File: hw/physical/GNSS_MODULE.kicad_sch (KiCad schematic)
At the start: 16 parts, among them J3 Conn_Coaxial, U3 MAX-M8C

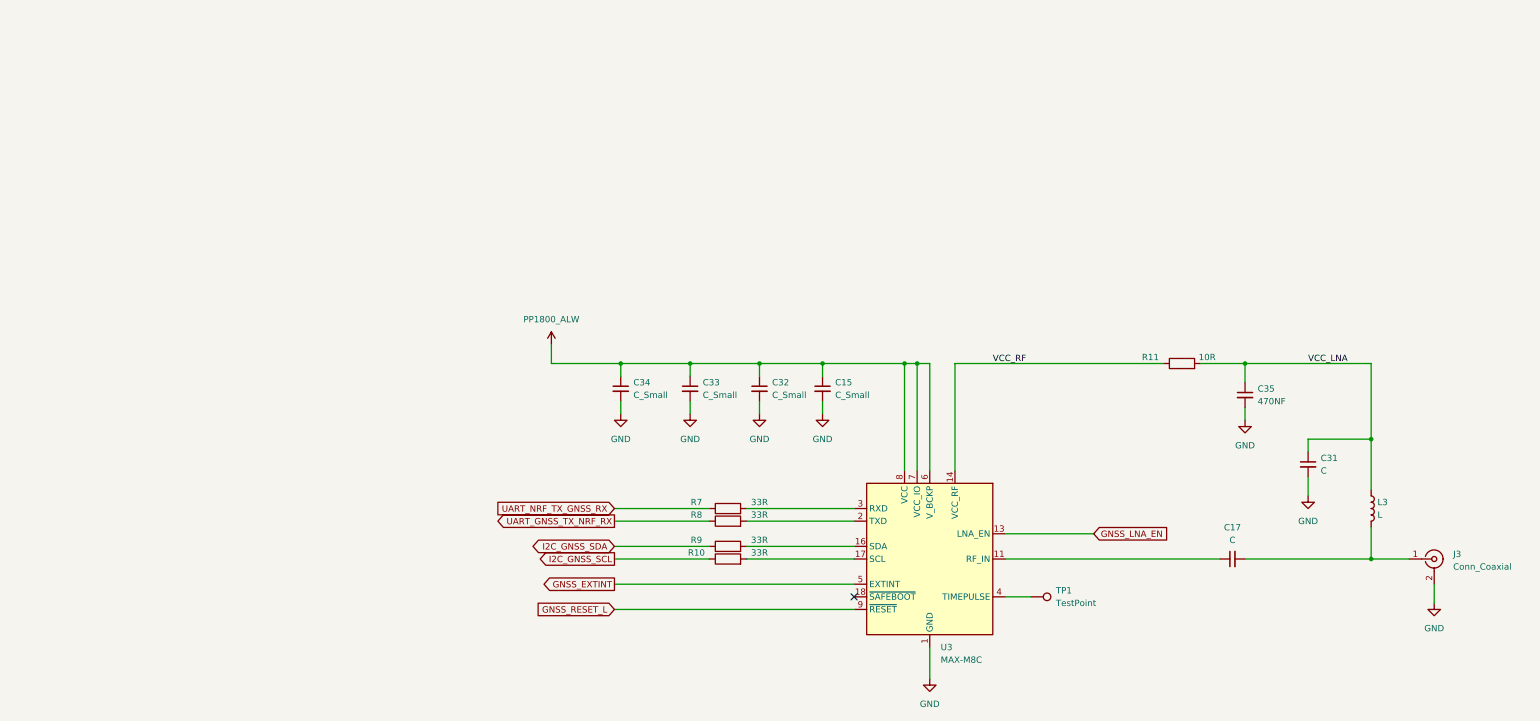
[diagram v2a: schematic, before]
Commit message: Various Schematic Modifications and Additions. * Removed Bypass page and moved bypass caps to MCU page. * Moved MCU VSS_PA pin to logical location as per Nordic guidelines. * Added Display Circuit, level shifters, charge pump, connector, etc. * Added 3.3V display VREG with Enable GPIO. * Added BLE RF components as per Nordic guidelines. * Added DCC circuit as per Nordic guidelines. * Rearranged GPIO's and interfaces. * Fixed various schematic errors.
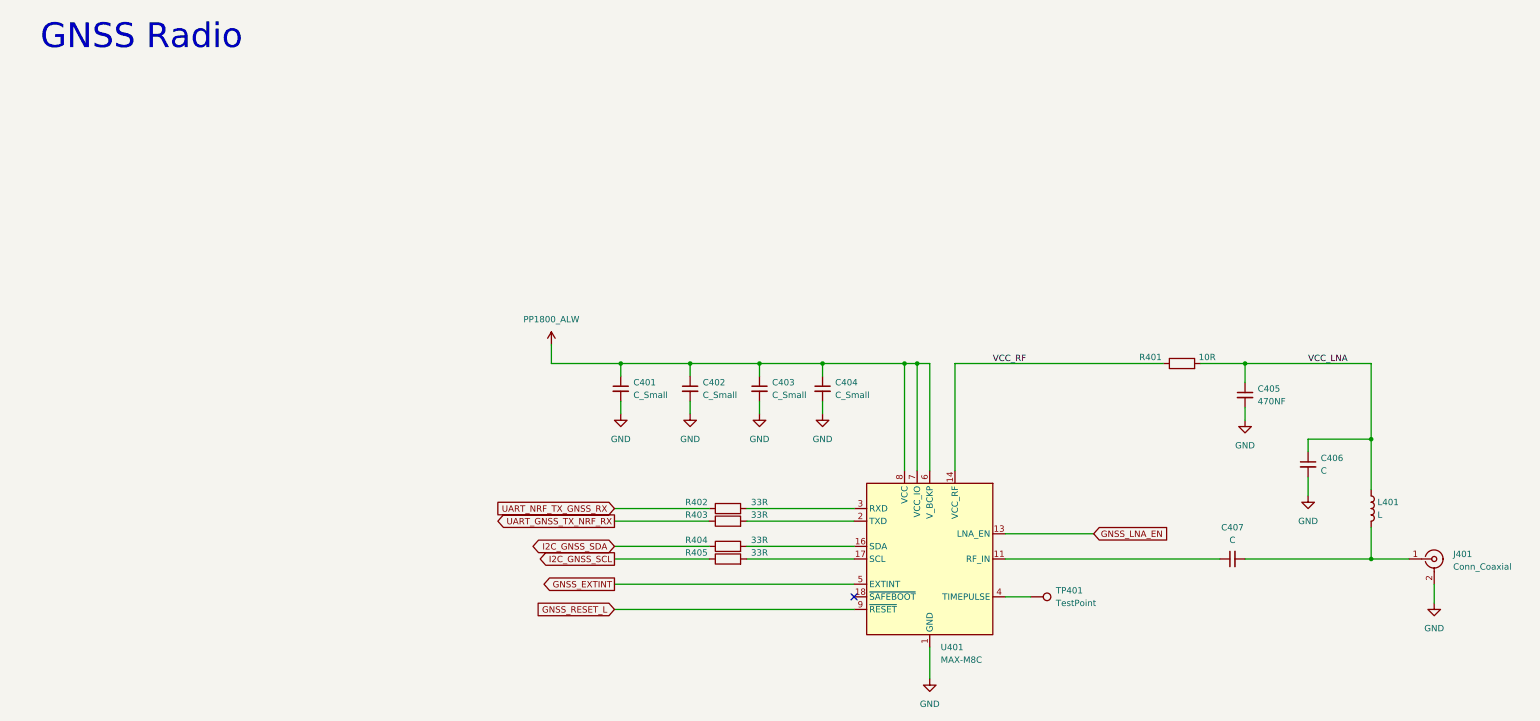
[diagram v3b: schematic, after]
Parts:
- renumbered C34 to C401, C33 to C402, C32 to C403, C15 to C404, C35 to C405, C31 to C406, C17 to C407, J3 to J401, L3 to L401, R11 to R401, R7 to R402, R8 to R403, R9 to R404, R10 to R405, TP1 to TP401, U3 to U401
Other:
- note added: "GNSS Radio"
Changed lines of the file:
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@@
+		)
+	)
+	(text "GNSS Radio"
+		(exclude_from_sim no)
+		(at 44.45 23.114 0)
+		(effects
+			(font
+				(size 5 5)
+			)
 		)
 	)
@@
 		(dnp no)
 		(fields_autoplaced yes)
-		(property "Reference" "#PWR038"
+		(property "Reference" "#PWR0408"
 			(at 304.8 143.51 0)
 			(effects
@@
 			(project "lora_radio_lp"
 				(path "/fff85bc4-e8ec-4b5d-b2e2-83ecb397a864/43b1fc22-b706-4706-a6f5-d4b7f0f9014a"
-					(reference "#PWR038")
+					(reference "#PWR0408")
 					(unit 1)
 				)
@@
 		(dnp no)
 		(fields_autoplaced yes)
-		(property "Reference" "#PWR035"
+		(property "Reference" "#PWR0409"
 			(at 203.2 158.75 0)
 			(effects
@@
 			(project "lora_radio_lp"
 				(path "/fff85bc4-e8ec-4b5d-b2e2-83ecb397a864/43b1fc22-b706-4706-a6f5-d4b7f0f9014a"
-					(reference "#PWR035")
+					(reference "#PWR0409")
 					(unit 1)
 				)
@@
 		(on_board yes)
 		(dnp no)
-		(property "Reference" "R9"
+		(property "Reference" "R404"
 			(at 156.21 124.46 90)
 			(effects
@@
 			(project "lora_radio_lp"
 				(path "/fff85bc4-e8ec-4b5d-b2e2-83ecb397a864/43b1fc22-b706-4706-a6f5-d4b7f0f9014a"
-					(reference "R9")
+					(reference "R404")
 					(unit 1)
 				)
@@
 		(dnp no)
 		(fields_autoplaced yes)
-		(property "Reference" "#PWR061"
+		(property "Reference" "#PWR0402"
 			(at 140.97 105.41 0)
 			(effects
@@
 			(project "lora_radio_lp"
 				(path "/fff85bc4-e8ec-4b5d-b2e2-83ecb397a864/43b1fc22-b706-4706-a6f5-d4b7f0f9014a"
-					(reference "#PWR061")
+					(reference "#PWR0402")
 					(unit 1)
 				)
@@
 		(on_board yes)
 		(dnp no)
-		(property "Reference" "R7"
+		(property "Reference" "R402"
 			(at 156.21 116.84 90)
 			(effects
@@
 			(project "lora_radio_lp"
 				(path "/fff85bc4-e8ec-4b5d-b2e2-83ecb397a864/43b1fc22-b706-4706-a6f5-d4b7f0f9014a"
-					(reference "R7")
+					(reference "R402")
 					(unit 1)
 				)
@@
 		(dnp no)
 		(fields_autoplaced yes)
-		(property "Reference" "C33"
+		(property "Reference" "C402"
 			(at 157.48 92.7162 0)
 			(effects
@@
 			(project "lora_radio_lp"
 				(path "/fff85bc4-e8ec-4b5d-b2e2-83ecb397a864/43b1fc22-b706-4706-a6f5-d4b7f0f9014a"
-					(reference "C33")
+					(reference "C402")
 					(unit 1)
 				)
@@
 		(dnp no)
 		(fields_autoplaced yes)
-		(property "Reference" "C34"
+		(property "Reference" "C401"
 			(at 143.51 92.7162 0)
 			(effects
@@
 			(project "lora_radio_lp"
 				(path "/fff85bc4-e8ec-4b5d-b2e2-83ecb397a864/43b1fc22-b706-4706-a6f5-d4b7f0f9014a"
-					(reference "C34")
+					(reference "C401")
 					(unit 1)
 				)
@@
 		(dnp no)
 		(fields_autoplaced yes)
-		(property "Reference" "#PWR059"
+		(property "Reference" "#PWR0407"
 			(at 279.4 121.92 0)
 			(effects
@@
 			(project "lora_radio_lp"
 				(path "/fff85bc4-e8ec-4b5d-b2e2-83ecb397a864/43b1fc22-b706-4706-a6f5-d4b7f0f9014a"
-					(reference "#PWR059")
+					(reference "#PWR0407")
 					(unit 1)
 				)
@@
 		(dnp no)
 		(fields_autoplaced yes)
-		(property "Reference" "C35"
+		(property "Reference" "C405"
 			(at 269.24 93.9862 0)
 			(effects
@@
 			(project "lora_radio_lp"
 				(path "/fff85bc4-e8ec-4b5d-b2e2-83ecb397a864/43b1fc22-b706-4706-a6f5-d4b7f0f9014a"
-					(reference "C35")
+					(reference "C405")
 					(unit 1)
 				)
@@
 		(dnp no)
 		(fields_autoplaced yes)
-		(property "Reference" "TP1"
+		(property "Reference" "TP401"
 			(at 228.6 134.6199 90)
 			(effects
@@
 			(project "lora_radio_lp"
 				(path "/fff85bc4-e8ec-4b5d-b2e2-83ecb397a864/43b1fc22-b706-4706-a6f5-d4b7f0f9014a"
-					(reference "TP1")
+					(reference "TP401")
 					(unit 1)
 				)
@@
 		(dnp no)
 		(fields_autoplaced yes)
-		(property "Reference" "L3"
+		(property "Reference" "L401"
 			(at 293.37 116.8399 0)
 			(effects
@@
 			(project "lora_radio_lp"
 				(path "/fff85bc4-e8ec-4b5d-b2e2-83ecb397a864/43b1fc22-b706-4706-a6f5-d4b7f0f9014a"
-					(reference "L3")
+					(reference "L401")
 					(unit 1)
 				)
@@
 		(dnp no)
 		(fields_autoplaced yes)
-		(property "Reference" "#PWR029"
+		(property "Reference" "#PWR0405"
 			(at 181.61 105.41 0)
 			(effects
@@
 			(project "lora_radio_lp"
 				(path "/fff85bc4-e8ec-4b5d-b2e2-83ecb397a864/43b1fc22-b706-4706-a6f5-d4b7f0f9014a"
-					(reference "#PWR029")
+					(reference "#PWR0405")
 					(unit 1)
 				)
@@
 		(dnp no)
 		(fields_autoplaced yes)
-		(property "Reference" "#PWR062"
+		(property "Reference" "#PWR0406"
 			(at 266.7 106.68 0)
 			(effects
@@
 			(project "lora_radio_lp"
 				(path "/fff85bc4-e8ec-4b5d-b2e2-83ecb397a864/43b1fc22-b706-4706-a6f5-d4b7f0f9014a"
-					(reference "#PWR062")
+					(reference "#PWR0406")
 					(unit 1)
 				)
@@
 		(dnp no)
 		(fields_autoplaced yes)
-		(property "Reference" "J3"
+		(property "Reference" "J401"
 			(at 308.61 127.2931 0)
 			(effects
@@
 			(project "lora_radio_lp"
 				(path "/fff85bc4-e8ec-4b5d-b2e2-83ecb397a864/43b1fc22-b706-4706-a6f5-d4b7f0f9014a"
-					(reference "J3")
+					(reference "J401")
 					(unit 1)
 				)
@@
 		(on_board yes)
 		(dnp no)
-		(property "Reference" "R10"
+		(property "Reference" "R405"
 			(at 156.21 127 90)
 			(effects
@@
 			(project "lora_radio_lp"
 				(path "/fff85bc4-e8ec-4b5d-b2e2-83ecb397a864/43b1fc22-b706-4706-a6f5-d4b7f0f9014a"
-					(reference "R10")
+					(reference "R405")
 					(unit 1)
 				)
@@
 		(on_board yes)
 		(dnp no)
-		(property "Reference" "R8"
+		(property "Reference" "R403"
 			(at 156.21 119.38 90)
 			(effects
@@
 			(project "lora_radio_lp"
 				(path "/fff85bc4-e8ec-4b5d-b2e2-83ecb397a864/43b1fc22-b706-4706-a6f5-d4b7f0f9014a"
-					(reference "R8")
+					(reference "R403")
 					(unit 1)
 				)
@@
 		(dnp no)
 		(fields_autoplaced yes)
-		(property "Reference" "#PWR060"
+		(property "Reference" "#PWR0403"
 			(at 154.94 105.41 0)
 			(effects
@@
 			(project "lora_radio_lp"
 				(path "/fff85bc4-e8ec-4b5d-b2e2-83ecb397a864/43b1fc22-b706-4706-a6f5-d4b7f0f9014a"
-					(reference "#PWR060")
+					(reference "#PWR0403")
 					(unit 1)
 				)
@@
 		(dnp no)
 		(fields_autoplaced yes)
-		(property "Reference" "#PWR036"
+		(property "Reference" "#PWR0404"
 			(at 168.91 105.41 0)
 			(effects
@@
 			(project "lora_radio_lp"
 				(path "/fff85bc4-e8ec-4b5d-b2e2-83ecb397a864/43b1fc22-b706-4706-a6f5-d4b7f0f9014a"
-					(reference "#PWR036")
+					(reference "#PWR0404")
 					(unit 1)
 				)
@@
 		(dnp no)
 		(fields_autoplaced yes)
-		(property "Reference" "C15"
+		(property "Reference" "C404"
 			(at 184.15 92.7162 0)
 			(effects
@@
 			(project "lora_radio_lp"
 				(path "/fff85bc4-e8ec-4b5d-b2e2-83ecb397a864/43b1fc22-b706-4706-a6f5-d4b7f0f9014a"
-					(reference "C15")
+					(reference "C404")
 					(unit 1)
 				)
@@
 		(dnp no)
 		(fields_autoplaced yes)
-		(property "Reference" "U3"
+		(property "Reference" "U401"
 			(at 205.3941 146.05 0)
 			(effects
@@
 			(project "lora_radio_lp"
 				(path "/fff85bc4-e8ec-4b5d-b2e2-83ecb397a864/43b1fc22-b706-4706-a6f5-d4b7f0f9014a"
-					(reference "U3")
+					(reference "U401")
 					(unit 1)
 				)
@@
 		(dnp no)
 		(fields_autoplaced yes)
-		(property "Reference" "C17"
+		(property "Reference" "C407"
 			(at 264.1663 121.92 90)
 			(effects
@@
 			(project "lora_radio_lp"
 				(path "/fff85bc4-e8ec-4b5d-b2e2-83ecb397a864/43b1fc22-b706-4706-a6f5-d4b7f0f9014a"
-					(reference "C17")
+					(reference "C407")
 					(unit 1)
 				)
@@
 		(on_board yes)
 		(dnp no)
-		(property "Reference" "R11"
+		(property "Reference" "R401"
 			(at 247.65 87.63 90)
 			(effects
@@
 			(project "lora_radio_lp"
 				(path "/fff85bc4-e8ec-4b5d-b2e2-83ecb397a864/43b1fc22-b706-4706-a6f5-d4b7f0f9014a"
-					(reference "R11")
+					(reference "R401")
 					(unit 1)
 				)
@@
 		(dnp no)
 		(fields_autoplaced yes)
-		(property "Reference" "C32"
+		(property "Reference" "C403"
 			(at 171.45 92.7162 0)
 			(effects
@@
 			(project "lora_radio_lp"
 				(path "/fff85bc4-e8ec-4b5d-b2e2-83ecb397a864/43b1fc22-b706-4706-a6f5-d4b7f0f9014a"
-					(reference "C32")
+					(reference "C403")
 					(unit 1)
 				)
@@
 		(dnp no)
 		(fields_autoplaced yes)
-		(property "Reference" "C31"
+		(property "Reference" "C406"
 			(at 281.94 107.9562 0)
 			(effects
@@
 			(project "lora_radio_lp"
 				(path "/fff85bc4-e8ec-4b5d-b2e2-83ecb397a864/43b1fc22-b706-4706-a6f5-d4b7f0f9014a"
-					(reference "C31")
-					(unit 1)
-				)
+					(reference "C406")
+					(unit 1)
+				)
